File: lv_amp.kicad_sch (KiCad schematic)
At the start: 84 parts, among them J1 Jack-DC, J2 AudioJack2, J3 AudioJack2, Q1 Q_NMOS_DGS, U1 MAX1771xSA, U2 TL072, U3 ECC83, U4 ECC83, U5 ECC83

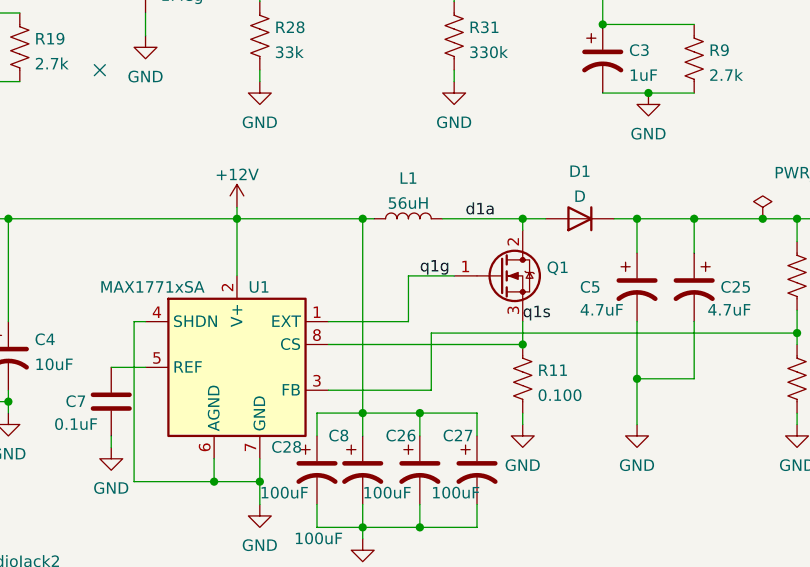
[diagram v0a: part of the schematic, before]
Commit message: alpha0 errata: add gate resistor for switching mosfet
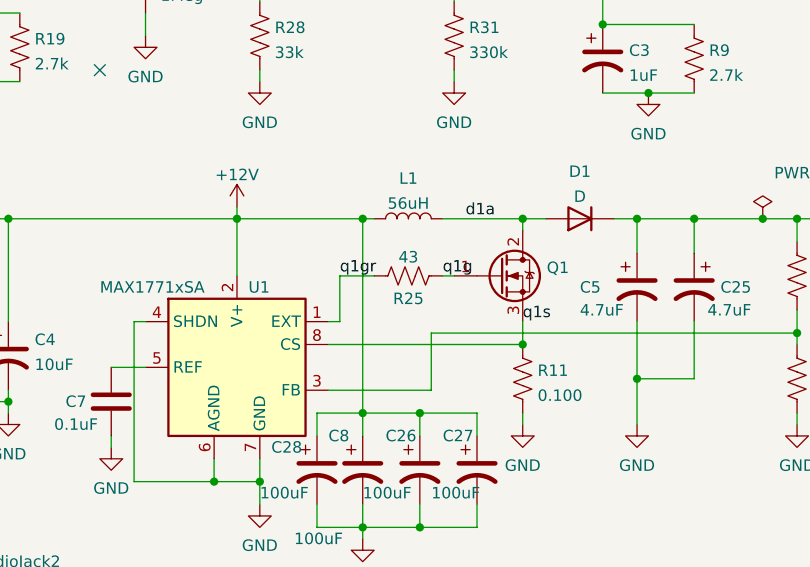
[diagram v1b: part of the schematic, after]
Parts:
- added R25: 43, Resistor_SMD:R_0603_1608Metric, symbol Device:R_US
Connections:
- net q1g: now also R25.2; no longer U1.1 (EXT)
- new net q1gr: R25.1, U1.1 (EXT)
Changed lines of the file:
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@@
     (stroke (width 0) (type default) (color 0 0 0 0))
   )
-  (wire (pts (xy 160.02 130.81) (xy 168.91 130.81))
-    (stroke (width 0) (type default) (color 0 0 0 0))
-  )
   (wire (pts (xy 163.83 153.67) (xy 163.83 154.94))
     (stroke (width 0) (type default) (color 0 0 0 0))
@@
     (stroke (width 0) (type default) (color 0 0 0 0))
   )
-  (wire (pts (xy 168.91 130.81) (xy 168.91 125.73))
-    (stroke (width 0) (type default) (color 0 0 0 0))
-  )
   (wire (pts (xy 115.57 104.14) (xy 120.65 104.14))
     (stroke (width 0) (type default) (color 0 0 0 0))
@@
     (stroke (width 0) (type default) (color 0 0 0 0))
   )
-  (wire (pts (xy 168.91 125.73) (xy 173.99 125.73))
+  (wire (pts (xy 172.72 125.73) (xy 173.99 125.73))
     (stroke (width 0) (type default) (color 0 0 0 0))
   )
@@
     (stroke (width 0) (type default) (color 0 0 0 0))
   )
+  (wire (pts (xy 161.29 125.73) (xy 161.29 130.81))
+    (stroke (width 0) (type default) (color 0 0 0 0))
+  )
   (wire (pts (xy 200.66 119.38) (xy 208.28 119.38))
     (stroke (width 0) (type default) (color 0 0 0 0))
@@
     (stroke (width 0) (type default) (color 0 0 0 0))
   )
+  (wire (pts (xy 161.29 130.81) (xy 160.02 130.81))
+    (stroke (width 0) (type default) (color 0 0 0 0))
+  )
   (wire (pts (xy 118.11 40.64) (xy 118.11 44.45))
     (stroke (width 0) (type default) (color 0 0 0 0))
@@
     (stroke (width 0) (type default) (color 0 0 0 0))
   )
+  (wire (pts (xy 165.1 125.73) (xy 161.29 125.73))
+    (stroke (width 0) (type default) (color 0 0 0 0))
+  )
   (wire (pts (xy 212.09 129.54) (xy 212.09 132.08))
     (stroke (width 0) (type default) (color 0 0 0 0))
@@
     (effects (font (size 1.27 1.27)) (justify left bottom))
   )
-  (label "q1g" (at 170.18 125.73 0)
+  (label "q1g" (at 172.72 125.73 0)
     (effects (font (size 1.27 1.27)) (justify left bottom))
   )
@@
     (effects (font (size 1.27 1.27)) (justify left bottom))
   )
+  (label "q1gr" (at 161.29 125.73 0)
+    (effects (font (size 1.27 1.27)) (justify left bottom))
+  )
   (label "u3bp" (at 199.39 69.85 0)
     (effects (font (size 1.27 1.27)) (justify left bottom))
@@
     (pin "2")
   )
+  (symbol (lib_id "Device:R_US") (at 168.91 125.73 90) (unit 1)
+    (in_bom yes) (on_board yes)
+    (property "Reference" "R25" (id 0) (at 168.91 128.27 90))
+    (property "Value" "43" (id 1) (at 168.91 123.6496 90))
+    (property "Footprint" "Resistor_SMD:R_0603_1608Metric" (id 2) (at 169.164 124.714 90)
+      (effects (font (size 1.27 1.27)) hide)
+    )
+    (property "Datasheet" "~" (id 3) (at 168.91 125.73 0)
+      (effects (font (size 1.27 1.27)) hide)
+    )
+    (pin "1")
+    (pin "2")
+  )
   (symbol (lib_id "Device:C") (at 46.99 160.02 90) (unit 1)
     (in_bom yes) (on_board yes) (fields_autoplaced)
@@
       (reference "R24") (unit 1) (value "68k") (footprint "Resistor_SMD:R_0603_1608Metric")
     )
+    (path "/9ff3546c-fef5-4000-952e-477cc0de43ea"
+      (reference "R25") (unit 1) (value "43") (footprint "Resistor_SMD:R_0603_1608Metric")
+    )
     (path "/413fa014-254c-4b9e-a537-06e0dc8d85fa"

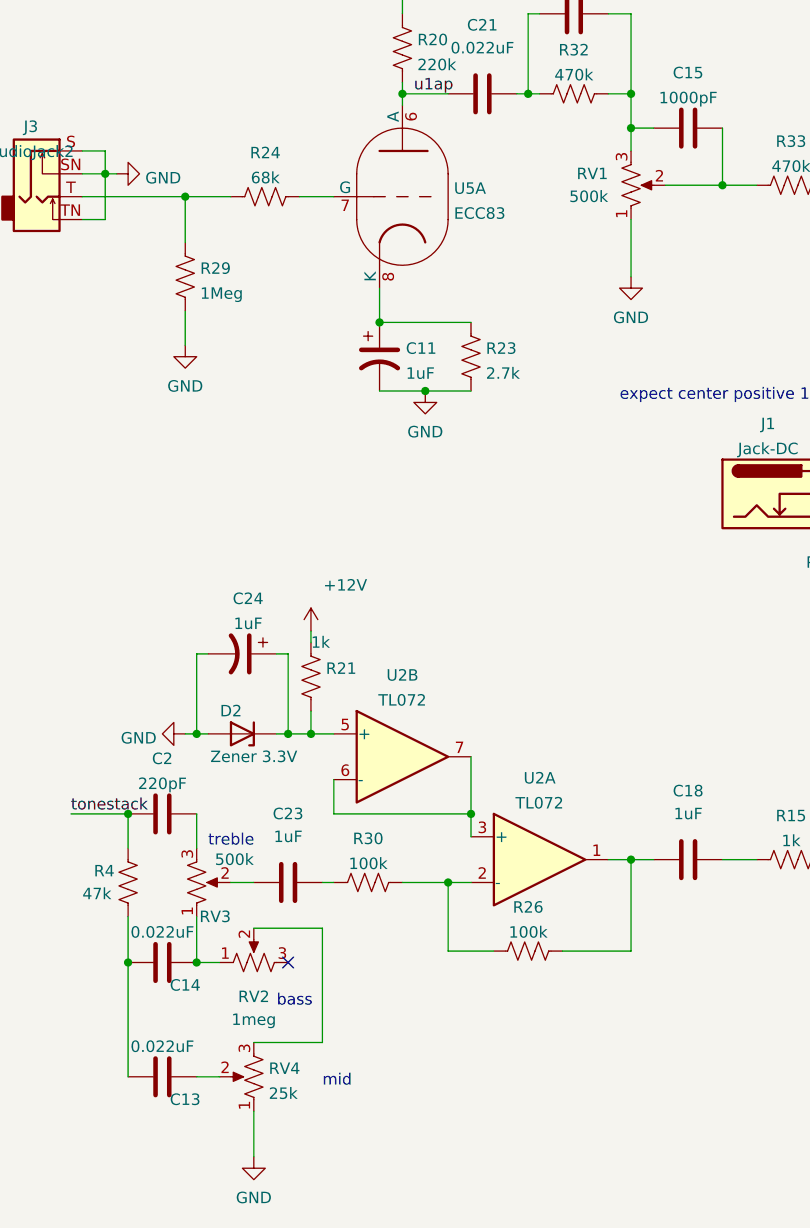
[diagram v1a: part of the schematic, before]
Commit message: alpha0 errata: note taper for pots
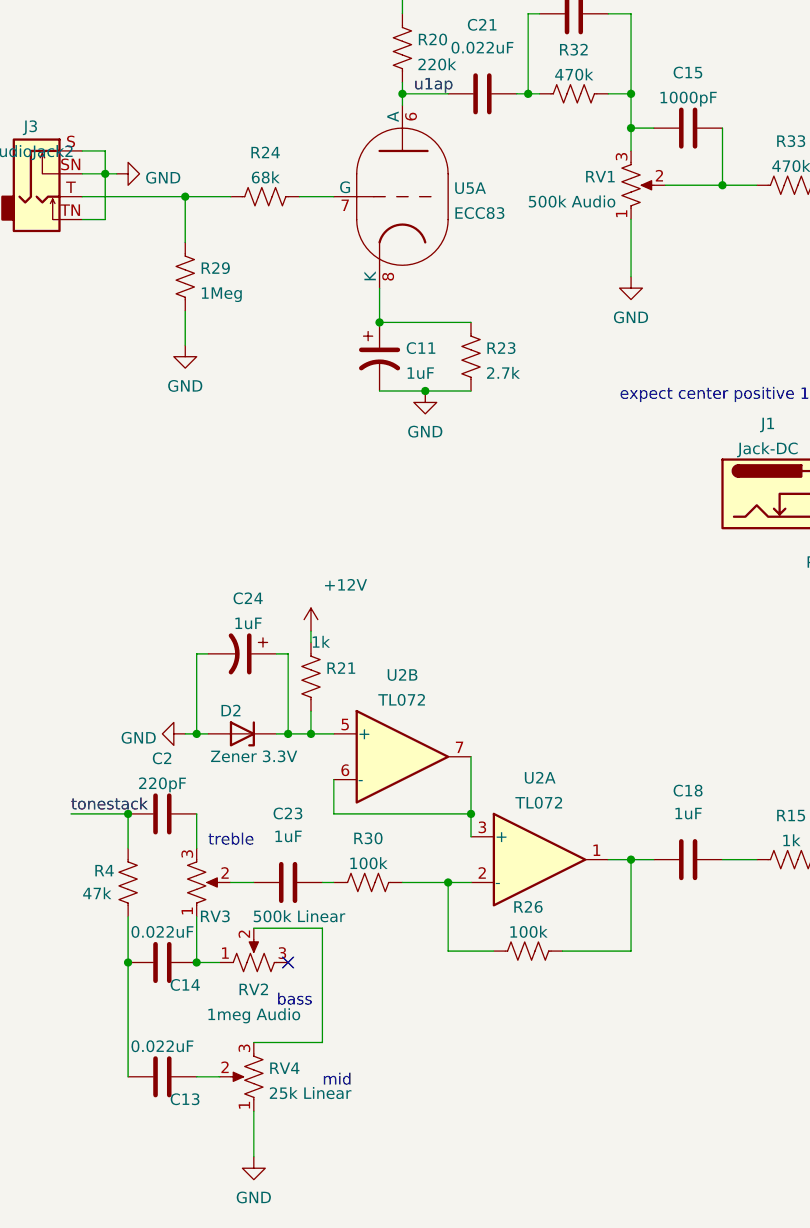
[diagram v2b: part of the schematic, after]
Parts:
- RV1: value 500k -> 500k Audio
- RV2: value 1meg -> 1meg Audio
- RV3: value 500k -> 500k Linear
- RV4: value 25k -> 25k Linear
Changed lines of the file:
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@@
   (symbol (lib_id "Device:R_Potentiometer_US") (at 85.09 82.55 0) (mirror x) (unit 1)
     (in_bom yes) (on_board yes) (fields_autoplaced)
-    (property "Reference" "RV1" (id 0) (at 82.55 81.2799 0)
+    (property "Reference" "RV1" (id 0) (at 83.439 81.6415 0)
       (effects (font (size 1.27 1.27)) (justify right))
     )
-    (property "Value" "500k" (id 1) (at 82.55 83.8199 0)
+    (property "Value" "500k Audio" (id 1) (at 83.439 84.4166 0)
       (effects (font (size 1.27 1.27)) (justify right))
     )
@@
   (symbol (lib_id "Device:R_Potentiometer_US") (at 43.18 168.91 90) (unit 1)
     (in_bom yes) (on_board yes) (fields_autoplaced)
-    (property "Reference" "RV2" (id 0) (at 43.18 172.72 90))
-    (property "Value" "1meg" (id 1) (at 43.18 175.26 90))
+    (property "Reference" "RV2" (id 0) (at 43.18 171.9485 90))
+    (property "Value" "1meg Audio" (id 1) (at 43.18 174.7236 90))
     (property "Footprint" "Potentiometer_THT:Potentiometer_Piher_T-16H_Single_Horizontal" (id 2) (at 43.18 168.91 0)
       (effects (font (size 1.27 1.27)) hide)
@@
       (effects (font (size 1.27 1.27)) (justify right))
     )
-    (property "Value" "25k" (id 1) (at 44.831 183.4766 0)
+    (property "Value" "25k Linear" (id 1) (at 44.831 183.4766 0)
       (effects (font (size 1.27 1.27)) (justify right))
     )
@@
       (effects (font (size 1.27 1.27)) (justify right))
     )
-    (property "Value" "500k" (id 1) (at 43.18 157.48 0)
+    (property "Value" "500k Linear" (id 1) (at 53.34 163.83 0)
       (effects (font (size 1.27 1.27)) (justify right))
     )
@@
     )
     (path "/4537a5c1-2eca-45e3-824f-5f450b04aaa3"
-      (reference "RV1") (unit 1) (value "500k") (footprint "Potentiometer_THT:Potentiometer_Piher_T-16H_Single_Horizontal")
+      (reference "RV1") (unit 1) (value "500k Audio") (footprint "Potentiometer_THT:Potentiometer_Piher_T-16H_Single_Horizontal")
     )
     (path "/4ccf9743-6a73-4d51-9824-885bca1d6343"
-      (reference "RV2") (unit 1) (value "1meg") (footprint "Potentiometer_THT:Potentiometer_Piher_T-16H_Single_Horizontal")
+      (reference "RV2") (unit 1) (value "1meg Audio") (footprint "Potentiometer_THT:Potentiometer_Piher_T-16H_Single_Horizontal")
     )
     (path "/dff621bd-85c0-4427-a6dc-509957f4a0e4"
-      (reference "RV3") (unit 1) (value "500k") (footprint "Potentiometer_THT:Potentiometer_Piher_T-16H_Single_Horizontal")
+      (reference "RV3") (unit 1) (value "500k Linear") (footprint "Potentiometer_THT:Potentiometer_Piher_T-16H_Single_Horizontal")
     )
     (path "/bd63cb9b-a387-4c82-b5aa-91ecc6fedba2"
-      (reference "RV4") (unit 1) (value "25k") (footprint "Potentiometer_THT:Potentiometer_Piher_T-16H_Single_Horizontal")
+      (reference "RV4") (unit 1) (value "25k Linear") (footprint "Potentiometer_THT:Potentiometer_Piher_T-16H_Single_Horizontal")
     )
     (path "/de58a2a0-9e57-48c8-a39b-3127c73bef33"

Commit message: alpha0 errata: flip mid pot
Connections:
- net GND: now also RV4.3; no longer RV4.1
- net at RV2.2: now also RV4.1; no longer RV4.3
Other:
- moved on the sheet: RV4
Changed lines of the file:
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@@
     (pin "2")
   )
-  (symbol (lib_id "Device:R_Potentiometer_US") (at 43.18 181.61 180) (unit 1)
+  (symbol (lib_id "Device:R_Potentiometer_US") (at 43.18 181.61 0) (mirror y) (unit 1)
     (in_bom yes) (on_board yes) (fields_autoplaced)
     (property "Reference" "RV4" (id 0) (at 44.831 180.7015 0)

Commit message: alpha0 errata: reduce R18 to reduce stage 4 gain
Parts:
- R18: value 1Meg -> 100k
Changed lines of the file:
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@@
       (effects (font (size 1.27 1.27)) (justify right))
     )
-    (property "Value" "1Meg" (id 1) (at 141.351 94.5766 0)
+    (property "Value" "100k" (id 1) (at 141.351 94.5766 0)
       (effects (font (size 1.27 1.27)) (justify right))
     )
@@
     )
     (path "/7627ad07-126b-4f32-b824-4d9523bebf30"
-      (reference "R18") (unit 1) (value "1Meg") (footprint "Resistor_SMD:R_0603_1608Metric")
+      (reference "R18") (unit 1) (value "100k") (footprint "Resistor_SMD:R_0603_1608Metric")
     )
     (path "/ad487d33-6ba3-4b24-956a-c205b839a8be"

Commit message: alpha0 errata: increase r1 to 4.3k to increase output level
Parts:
- R1: value 1k -> 4.3k
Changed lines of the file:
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@@
       (effects (font (size 1.27 1.27)) (justify left))
     )
-    (property "Value" "1k" (id 1) (at 255.651 83.1466 0)
+    (property "Value" "4.3k" (id 1) (at 255.651 83.1466 0)
       (effects (font (size 1.27 1.27)) (justify left))
     )
@@
     )
     (path "/5afa3632-aa94-4ade-91b3-46d777bee7c4"
-      (reference "R1") (unit 1) (value "1k") (footprint "Resistor_SMD:R_0603_1608Metric")
+      (reference "R1") (unit 1) (value "4.3k") (footprint "Resistor_SMD:R_0603_1608Metric")
     )
     (path "/20f8c6df-c852-4ad1-8291-502daa86579b"

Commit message: alpha0 errata: decrease r12 to 27k to reduce stage 5 gain
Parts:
- R12: value 56k -> 27k
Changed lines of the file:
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@@
       (effects (font (size 1.27 1.27)) (justify right))
     )
-    (property "Value" "56k" (id 1) (at 223.901 98.3866 0)
+    (property "Value" "27k" (id 1) (at 223.901 98.3866 0)
       (effects (font (size 1.27 1.27)) (justify right))
     )
@@
     )
     (path "/75fb8a9f-33b8-470f-9782-9c7d5464513e"
-      (reference "R12") (unit 1) (value "56k") (footprint "Resistor_SMD:R_2512_6332Metric")
+      (reference "R12") (unit 1) (value "27k") (footprint "Resistor_SMD:R_2512_6332Metric")
     )
     (path "/f45e46e2-1eb0-4825-b2ff-ea4e427352f1"
